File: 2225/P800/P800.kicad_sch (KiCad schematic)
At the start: 29 parts, among them J1 Screw_Terminal_01x05, J2 Conn_Coaxial, J3 Conn_Coaxial, J4 Conn_Coaxial, J5 Conn_Coaxial

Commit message: Completed initial P800 board layout.
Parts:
- removed HS1: Heatsink_Pad, P800_footprint_library:heatsink_577202B04000G, symbol Mechanical:Heatsink_Pad
- added HS1: Heatsink, P800_footprint_library:heatsink_577202B00000G, symbol Mechanical:Heatsink
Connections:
- net +24VAC: now also C802.1, F1.2, H803.3, H804.3; no longer F1.1, J1.5 (Pin_5)
- new net: F1.1, J1.5 (Pin_5)
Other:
- note added: "HEATSINK ON H805 (TO-220-3)"

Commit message: Replaced custom capacitor footprints with kicad standard footprints
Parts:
- C002, C003: footprint P800_footprint_library:cap_electrolytic_A50 -> Capacitor_THT:CP_Radial_D25.0mm_P10.00mm_SnapIn
- C803, C804: footprint P800_footprint_library:cap_electrolytic_UKW1J471MHD1TO -> Capacitor_THT:CP_Radial_D12.5mm_P5.00mm
- C805: footprint P800_footprint_library:cap_electrolytic_UFG1H101MPM1TD -> Capacitor_THT:CP_Radial_D10.0mm_P5.00mm
- C808: footprint P800_footprint_library:cap_electrolytic_panasonic_5X11 -> Capacitor_THT:CP_Radial_D5.0mm_P2.00mm
- C809: footprint P800_footprint_library:cap_electrolytic_UFG1C471MPM1TD -> Capacitor_THT:C_Radial_D10.0mm_H20.0mm_P5.00mm
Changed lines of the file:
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@@
 			)
 		)
-		(property "Footprint" "P800_footprint_library:cap_electrolytic_UFG1H101MPM1TD"
+		(property "Footprint" "Capacitor_THT:CP_Radial_D10.0mm_P5.00mm"
 			(at 130.81 114.3 0)
 			(effects
@@
 			)
 		)
-		(property "Footprint" "P800_footprint_library:cap_electrolytic_UKW1J471MHD1TO"
+		(property "Footprint" "Capacitor_THT:CP_Radial_D12.5mm_P5.00mm"
 			(at 121.92 114.3 0)
 			(effects
@@
 			)
 		)
-		(property "Footprint" "P800_footprint_library:cap_electrolytic_panasonic_5X11"
+		(property "Footprint" "Capacitor_THT:CP_Radial_D5.0mm_P2.00mm"
 			(at 179.07 90.17 0)
 			(effects
@@
 			)
 		)
-		(property "Footprint" "P800_footprint_library:cap_electrolytic_A50"
+		(property "Footprint" "Capacitor_THT:CP_Radial_D25.0mm_P10.00mm_SnapIn"
 			(at 181.61 72.39 0)
 			(effects
@@
 			)
 		)
-		(property "Footprint" "P800_footprint_library:cap_electrolytic_UFG1C471MPM1TD"
+		(property "Footprint" "Capacitor_THT:C_Radial_D10.0mm_H20.0mm_P5.00mm"
 			(at 180.34 118.11 0)
 			(effects
@@
 			)
 		)
-		(property "Footprint" "P800_footprint_library:cap_electrolytic_UKW1J471MHD1TO"
+		(property "Footprint" "Capacitor_THT:CP_Radial_D12.5mm_P5.00mm"
 			(at 113.03 114.3 0)
 			(effects
@@
 			)
 		)
-		(property "Footprint" "P800_footprint_library:cap_electrolytic_A50"
+		(property "Footprint" "Capacitor_THT:CP_Radial_D25.0mm_P10.00mm_SnapIn"
 			(at 181.61 57.15 0)
 			(effects

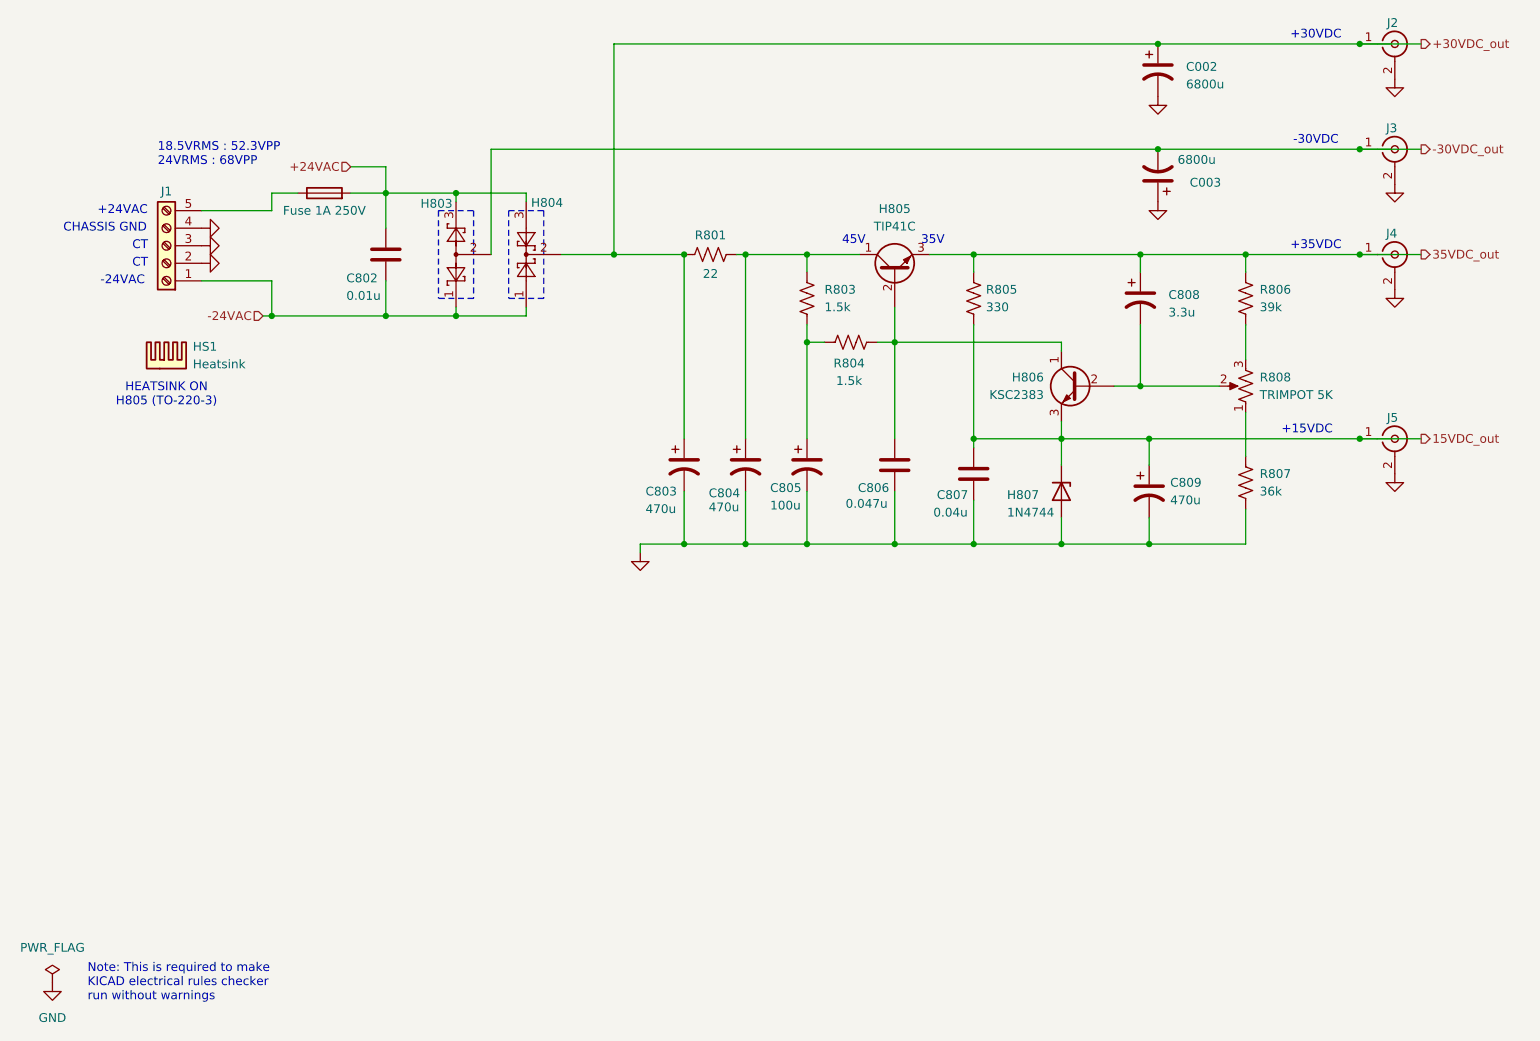
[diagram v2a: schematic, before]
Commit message: Redesigned P800 layout
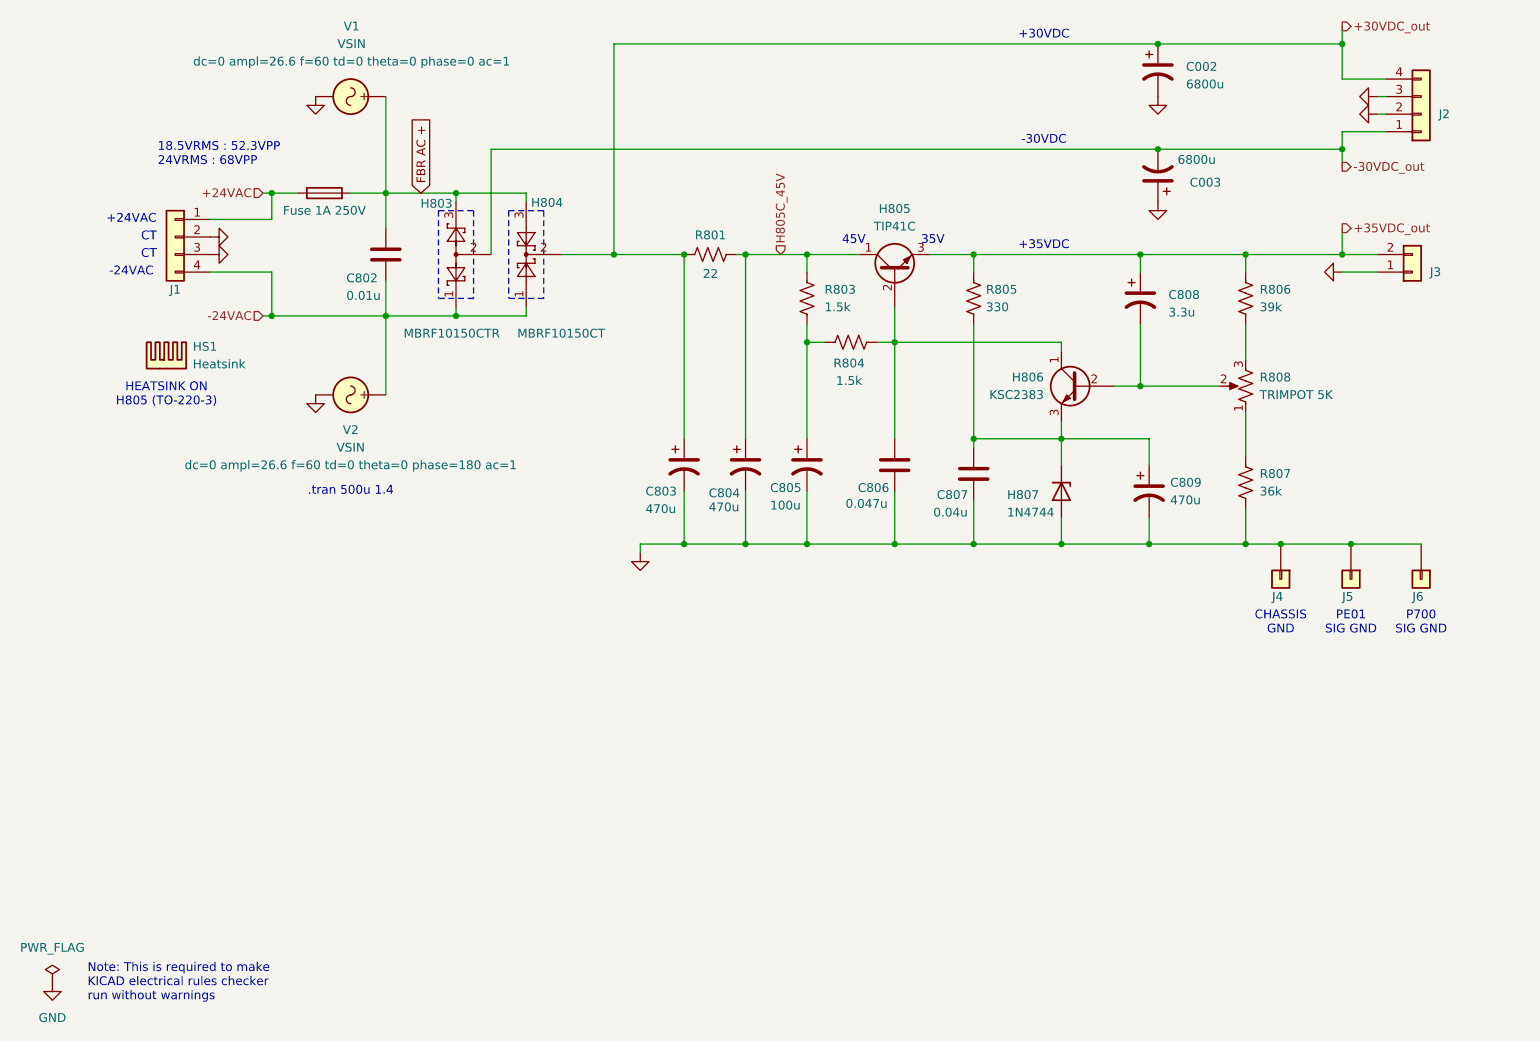
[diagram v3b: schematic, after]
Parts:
- removed J1: Screw_Terminal_01x05, P800_footprint_library:molex_5pos_connector_395443005, symbol Connector:Screw_Terminal_01x05
- removed J2, J3, J4, J5: Conn_Coaxial, P800_footprint_library:sma_connector_RFPC-SMA27-F, symbol Connector:Conn_Coaxial
- added J1, J2: Conn_01x04, P800_footprint_library:molex_nanofit_4-pos_header_1053131204, symbol Connector_Generic:Conn_01x04
- added J3: Conn_01x02, P800_footprint_library:molex_nanofit_2-pos_header_1053132302, symbol Connector_Generic:Conn_01x02
- added J4, J5, J6: Conn_01x01, P800_footprint_library:Metz_Connect_1pos_terminal_360291, symbol Connector_Generic:Conn_01x01
- added V1, V2: VSIN, symbol Simulation_SPICE:VSIN
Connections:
- net +24VAC: now also F1.1, J1.1 (Pin_1); no longer C802.1, F1.2, H803.3, H804.3
- net +30VDC_out: now also J2.4 (Pin_4)
- net -24VAC: now also J1.4 (Pin_4), V2.1
- net -30VDC_out: now also J2.1 (Pin_1)
- net GND: now also J1.2 (Pin_2), J1.3 (Pin_3), J2.2 (Pin_2), J2.3 (Pin_3), J3.1 (Pin_1), J4.1 (Pin_1), J5.1 (Pin_1), J6.1 (Pin_1), V1.2, V2.2
- net H805C_45V: now reaches C804.1, H805.1 (C), R801.2, R803.2
- net 15VDC_out: no longer names the net of C807.1, C809.1, H806.3 (E), H807.1 (K), R805.1
- net 35VDC_out renamed +35VDC_out
- net +35VDC_out: now also J3.2 (Pin_2)
- new net FBR AC +: C802.1, F1.2, H803.3, H804.3, V1.1
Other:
- note added: ".tran 500u 1.4"
- note added: "P700 SIG GND"
- note added: "PE01 SIG GND"
- note removed: "+15VDC"

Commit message: Changed molex connectors on P800 pcb from horizontal to vertical plug direction components
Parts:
- J1, J2: footprint P800_footprint_library:molex_nanofit_4-pos_header_1053131204 -> P800_footprint_library:molex_nanofit_4-pos_header_vert_1053091204
- J3: footprint P800_footprint_library:molex_nanofit_2-pos_header_1053132302 -> P800_footprint_library:molex_nanofit_2-pos_header_vert_1053091302
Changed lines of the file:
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@@
 			)
 		)
-		(property "Footprint" "P800_footprint_library:molex_nanofit_4-pos_header_1053131204"
+		(property "Footprint" "P800_footprint_library:molex_nanofit_4-pos_header_vert_1053091204"
 			(at 39.37 81.28 0)
 			(effects
@@
 			)
 		)
-		(property "Footprint" "P800_footprint_library:molex_nanofit_2-pos_header_1053132302"
+		(property "Footprint" "P800_footprint_library:molex_nanofit_2-pos_header_vert_1053091302"
 			(at 218.44 86.36 0)
 			(effects
@@
 			)
 		)
-		(property "Footprint" "P800_footprint_library:molex_nanofit_4-pos_header_1053131204"
+		(property "Footprint" "P800_footprint_library:molex_nanofit_4-pos_header_vert_1053091204"
 			(at 219.71 63.5 0)
 			(effects
